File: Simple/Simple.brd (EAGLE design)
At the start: 68.6 x 53.3 mm, 34 parts, among them IC1 LM7805, IC2 AVR-MEGA8-PPTH, IC3 MCP1700-33, J1 ISP, J4 VIN, Y1 16MHz

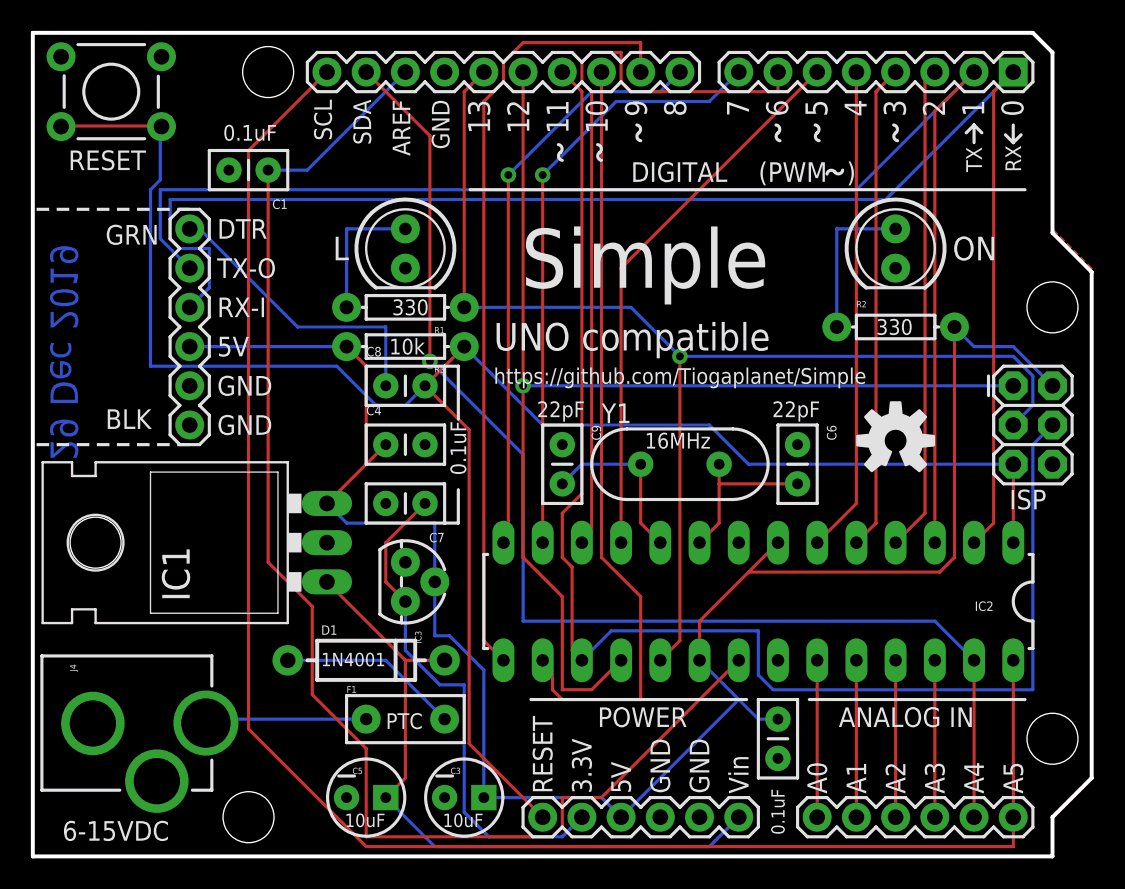
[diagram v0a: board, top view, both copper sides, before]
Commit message: Added IOREF and reserved pins
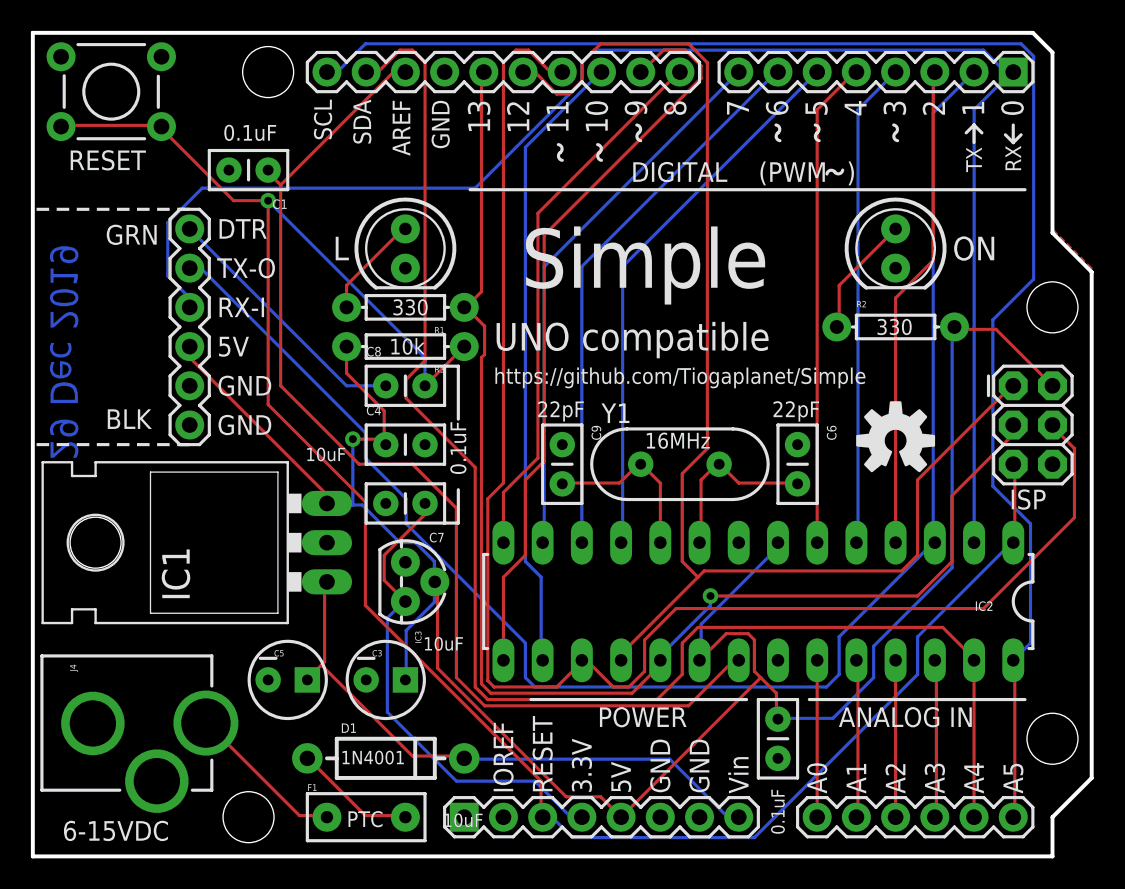
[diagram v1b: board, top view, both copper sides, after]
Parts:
- POWER: value (none) -> POWER; device SparkFun:1X06 -> SparkFun:1X08
- moved C3 9.16 mm to (22.9, 11.4)
- moved C5 9.16 mm to (16.5, 11.4)
- moved F1 6.84 mm to (21.6, 2.54)
- moved D1 6.48 mm to (22.9, 6.35)
- moved POWER 5.08 mm to (27.9, 2.54)
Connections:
- new net RESERVED: POWER.1
- net 3.3V: now also POWER.4; no longer POWER.2
- net 5V: now also POWER.5; no longer POWER.3
- net GND: now also POWER.6, POWER.7; no longer POWER.4, POWER.5
- net RESET: now also POWER.3; no longer POWER.1
- net VIN: now also POWER.8; no longer POWER.6
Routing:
- net AREF: track 87.3 -> 71.4 mm
- net 5V: track 124.0 -> 139.4 mm, vias 0 -> 1
- net AD4/SDA: track 80.2 -> 94.4 mm, vias 1 -> 0
- net IO6: track 48.0 -> 35.8 mm
- net AD5/SCL: track 109.4 -> 98.8 mm
- net SS: track 49.8 -> 40.6 mm
- net RESET: track 120.2 -> 128.4 mm, vias 0 -> 1
- net SCK: track 78.3 -> 86.4 mm
- net MISO: track 77.4 -> 85.4 mm, vias 1 -> 0
- net MOSI: track 90.6 -> 97.1 mm
- net TX-O: track 93.3 -> 99.6 mm
- net VIN: track 44.1 -> 38.1 mm
- net N$6: track 11.7 -> 7.91 mm
- net IO7: track 39.3 -> 35.8 mm, vias 1 -> 0
- net IO8: track 37.8 -> 35.2 mm, vias 1 -> 0
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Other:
- board text added: "IOREF"
